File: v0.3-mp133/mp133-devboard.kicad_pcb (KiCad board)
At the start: 4 copper layers, 39.9 x 57.9 mm, 146 parts, among them CON1 microSDCon_SMT_104031-0811, J1 Pins_02x40_P0.4mm_W3.0mm_SMT, J2 Pins_02x40_P0.4mm_W3.0mm_SMT, J3 USB-C_Receptacle_Molex_217179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, J4 Pins_02x04_RightAngle_P2.54mm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, J5 Conn_01x02, J6 Pins_02x05_P1.27mm_SMT, U13 NCP51460SN33, U14 DDR3L-RAM-4Gb_MT41K256M16TW, U15 AP6230xZ6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

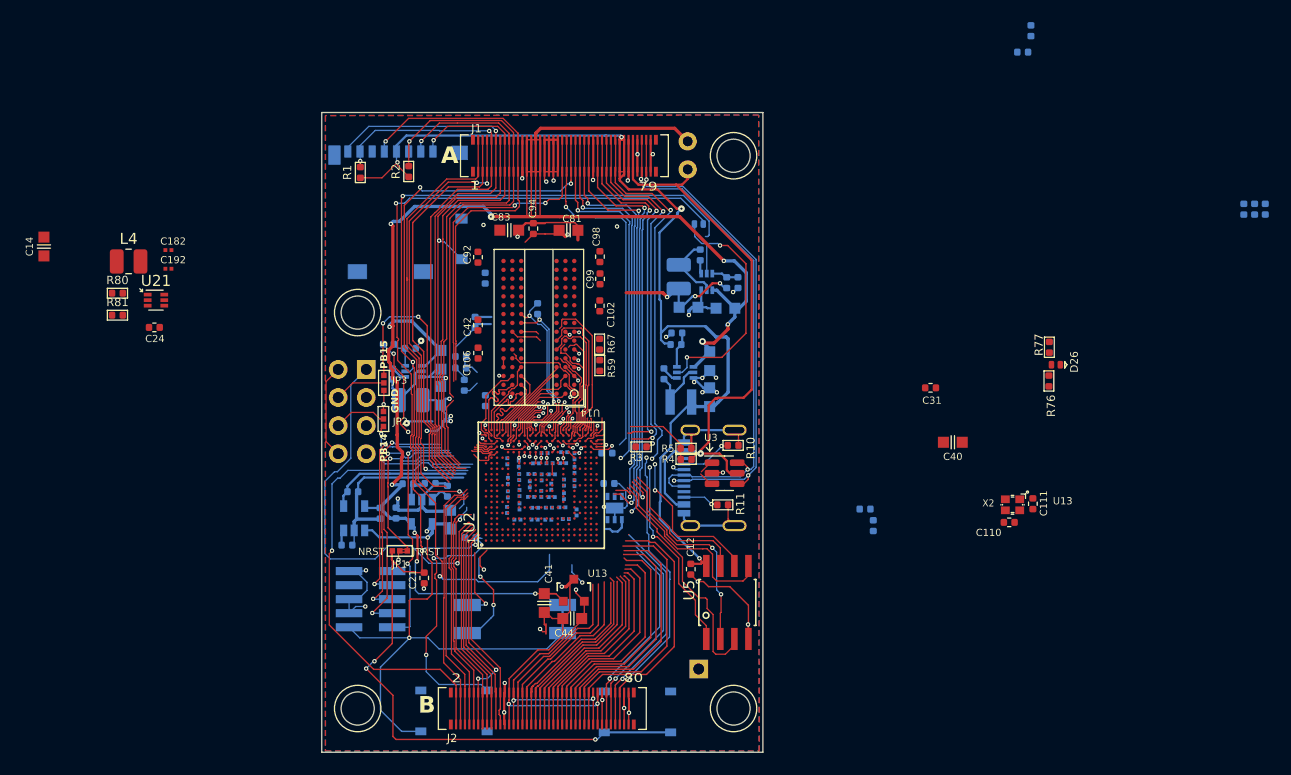
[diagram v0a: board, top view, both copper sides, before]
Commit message: mp13x: DDR3 RAM routed
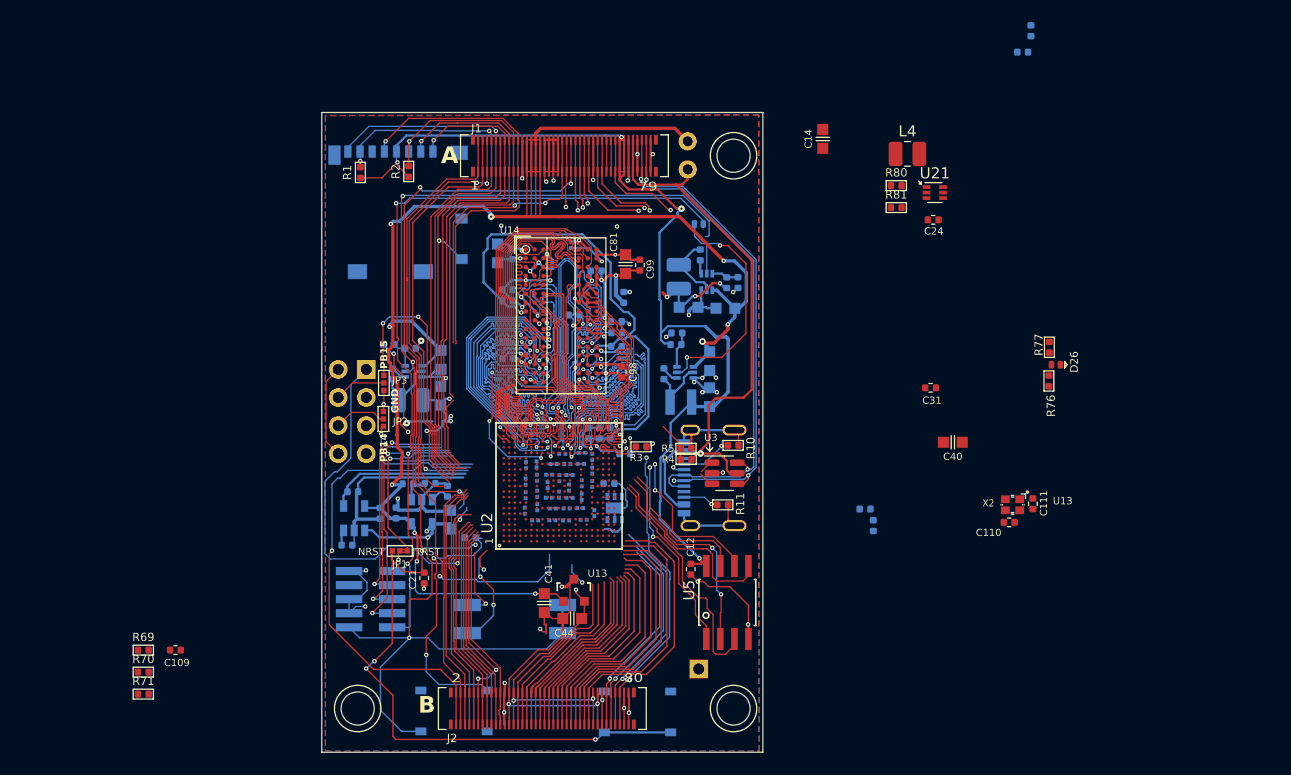
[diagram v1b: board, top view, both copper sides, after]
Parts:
- removed H2: Spacer Nylon, fits 3mm hole, 4ms_Hardware:MountingHole_Generic_3mm
- C102, C106, C182, C192, C42, C83, C92, C94, R59, R67: moved to B.Cu
- C109, R69, R70, R71: moved to F.Cu
- moved C14 71.1 mm to (234.5, 50.7)
- moved C24 71.1 mm to (244.5, 58.0)
- moved L4 71.1 mm to (242.1, 52.0)
- moved R80 71.1 mm to (241.1, 54.9)
- moved R81 71.1 mm to (241.1, 56.9)
- moved U21 71.1 mm to (244.6, 55.5)
- moved R78 62.6 mm to (215.2, 77.3)
- moved R79 62.6 mm to (214.2, 77.3)
- moved C13 62.6 mm to (213.3, 77.3)
- moved R71 41.9 mm to (173.0, 100.9)
- moved R70 38.9 mm to (173.0, 98.9), turned to 0 degrees
- moved R69 38.3 mm to (173.0, 96.9), turned to 0 degrees
- moved C182 36.4 mm to (211.7, 60.3), turned to -90 degrees
- moved C109 36.3 mm to (175.9, 96.9), turned to 0 degrees
- moved C192 34.7 mm to (210.0, 62.1), turned to 90 degrees
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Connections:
- C14 pad 2: +12V -> +5V
- U2 pad B21: /DDR_DQ2 -> /DDR_DQ0
- U2 pad D19: /DDR_DQ0 -> /DDR_DQ2
- U2 pad D20: /DDR_DQ7 -> /DDR_DQ5
- U2 pad F19: /DDR_DQ5 -> /DDR_DQ7
- U2 pad Y1: unconnected-(U2A-PA11-PadY1) -> /PA11
- U21 pad 1: +12V -> +5V
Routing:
- net VREF_DDR: track 8.46 -> 49.8 mm, vias 2 -> 3
- net /PD6: track 38.1 -> 5.88 mm, vias 2 -> 1
- net /PD12: track 33.0 -> 2.89 mm, vias 2 -> 0
- net /PE8: track 32.4 -> 2.89 mm, vias 2 -> 0
- net /PG10: track 38.5 -> 9.89 mm, vias 2 -> 1
- net GND: track 161.0 -> 189.3 mm, vias 49 -> 61
- net Net-(J1-Pin_57): track 37.7 -> 9.47 mm, vias 2 -> 1
- net Net-(J1-Pin_55): track 37.5 -> 9.50 mm, vias 2 -> 1
- net /PH12: track 33.3 -> 6.23 mm, vias 2 -> 1
- net /PE11: track 33.3 -> 6.47 mm, vias 2 -> 1
- net Net-(J1-Pin_41): track 32.2 -> 5.88 mm
- net /DDR_WEN: track 0.45 -> 25.2 mm, vias 1 -> 2
- net /DDR_A13: track 0.32 -> 25.0 mm, vias 1 -> 2
- net /DDR_A10: track 0.46 -> 24.9 mm, vias 1 -> 2
- net /DDR_CKE: track 0.95 -> 25.2 mm, vias 1 -> 2
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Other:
- board text added: "0"
- board text added: "0 mm"
- board text added: "0.01 mm"
- board text added: "0.02"
- board text added: "0.035 mm"
- board text added: "0.0900 mm / 0.0900 mm"
- board text added: "0.1 mm"
- board text added: "0.2000 mm"
- board text added: "1.24 mm"
- board text added: "1.6000 mm"
- board text added: "3.3"
- board text added: "39.9034 mm x 57.8692 mm"
- board text added: "4"
- board text added: "4.5"
- board text added: "B.Cu"
- board text added: "B.Mask"
- board text added: "B.Paste"
- board text added: "B.Silkscreen"
- board text added: "BOARD CHARACTERISTICS"
- board text added: "Board Thickness:"
- board text added: "Board overall dimensions:"
- board text added: "Bottom Silk Screen"
- board text added: "Bottom Solder Mask"
- board text added: "Bottom Solder Paste"
- board text added: "Castellated pads:"
- board text added: "Color"
- board text added: "Copper Finish:"
- board text added: "Copper Layer Count:"
- board text added: "Dielectric"
- board text added: "Edge card connectors:"
- board text added: "Epsilon R"
- board text added: "F.Cu"
- board text added: "F.Mask"
- board text added: "F.Paste"
- board text added: "F.Silkscreen"
- board text added: "FR4"
- board text added: "Impedance Control:"
- board text added: "In1.Cu"
- board text added: "In2.Cu"
- board text added: "Layer Name"
- board text added: "Loss Tangent"
- board text added: "Material"
- board text added: "Min hole diameter:"
- board text added: "Min track/spacing:"
- board text added: "No"
- board text added: "None"
- board text added: "Not specified"
- board text added: "Plated Board Edge:"
- board text added: "Thickness (mm)"
- board text added: "Top Silk Screen"
- board text added: "Top Solder Mask"
- board text added: "Top Solder Paste"
- board text added: "Type"
- board text added: "copper"
- board text added: "core"
- board text added: "prepreg"

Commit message: WIP Routing
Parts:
- added C1: 1uF_0201_4V, 4ms_Capacitor:C_0201, B.Cu at (213.7, 82.9)
- added H2: Spacer Nylon, fits 3mm hole, 4ms_Hardware:MountingHole_Generic_3mm, F.Cu at (192.4, 66.4)
- C109, C12, C14, C21, C24, C40, JP1, L4, R70, R71, R80, R81, U21, U5: moved to B.Cu
- moved R80 63.5 mm to (191.1, 93.9), turned to -90 degrees
- moved U21 63.4 mm to (192.4, 91.5), turned to -90 degrees
- moved C24 62.9 mm to (192.6, 93.5), turned to 180 degrees
- moved L4 61.8 mm to (195.0, 92.0), turned to 90 degrees
- moved R81 61.1 mm to (190.8, 91.5), turned to -90 degrees
- moved C14 57.6 mm to (191.5, 89.1), turned to 180 degrees
- moved C32 53.2 mm to (217.5, 80.3), turned to 180 degrees
- moved C40 52.6 mm to (194.8, 89.1), turned to 0 degrees
- moved C29 52.2 mm to (217.4, 81.4)
- moved R71 46.6 mm to (203.0, 65.2), turned to 180 degrees
- moved R70 46.4 mm to (204.5, 64.8), turned to 90 degrees
- moved C109 42.5 mm to (203.0, 64.2)
- moved R69 38.0 mm to (203.9, 74.8), turned to 90 degrees
- moved J6 31.0 mm to (224.5, 91.5)
- moved JP1 30.1 mm to (226.3, 87.1)
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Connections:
- J2 pad 35: Net-(J2-Pin_35) -> /PB1
- J2 pad 36: Net-(J2-Pin_35) -> /PB1
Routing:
- net /NRST: track 117.5 -> 12.0 mm, vias 6 -> 0
- net /UART_TX: track 35.9 -> 0.00 mm, vias 1 -> 0
- net GND: track 189.3 -> 222.7 mm, vias 61 -> 80
- net /PWR_ON: track 80.1 -> 50.3 mm
- net VDD_CPU: track 0.00 -> 26.2 mm, vias 0 -> 4
- net /DFU_BOOT: track 23.5 -> 0.01 mm, vias 2 -> 0
- net /JTCK_SWCLK: track 23.2 -> 0.00 mm, vias 2 -> 0
- net /JTDO_SWO: track 25.1 -> 3.38 mm, vias 3 -> 1
- net /PG1: track 18.8 -> 0.00 mm
- net /JTDI: track 21.0 -> 2.72 mm, vias 3 -> 1
- net VDD: track 60.6 -> 77.9 mm, vias 3 -> 16
- net /JTMS_SWDIO: track 21.5 -> 4.31 mm, vias 2 -> 0
- net /PH11: track 20.0 -> 2.89 mm, vias 2 -> 0
- net Net-(J2-Pin_35): track 16.9 -> 0.00 mm
- net /PB1: track 0.00 -> 16.9 mm
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- added copper zone on In1.Cu, net GND
- added copper zone on In2.Cu, net GND
- removed copper zone on In2.Cu, net VDD

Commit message: WIP routing
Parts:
- removed C30: 100nF_0402_16V, 4ms_Capacitor:C_0402
- C31, R76: moved to B.Cu
- C45, C72, C84, U18: moved to F.Cu
- moved R76 66.1 mm to (193.3, 96.6), turned to 180 degrees
- moved D26 65.1 mm to (191.9, 84.9)
- moved R77 64.5 mm to (192.0, 83.8), turned to 180 degrees
- moved TP1 42.1 mm to (227.0, 56.6)
- moved C110 41.3 mm to (210.3, 89.2), turned to -90 degrees
- moved C111 40.0 mm to (213.9, 89.0)
- moved X2 39.9 mm to (212.1, 89.1)
- moved R63 39.0 mm to (191.9, 95.0), turned to -90 degrees
- moved R64 38.9 mm to (191.3, 93.0), turned to -90 degrees
- moved C48 37.4 mm to (192.8, 91.1), turned to 180 degrees
- moved U16 35.5 mm to (193.9, 93.4), turned to -90 degrees
- moved C68 35.1 mm to (194.0, 95.3), turned to 180 degrees
- moved C72 35.0 mm to (225.8, 94.1), turned to 180 degrees
- moved C84 34.0 mm to (225.3, 89.3), turned to 0 degrees
- moved U18 33.7 mm to (225.2, 91.7)
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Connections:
- J2 pad 29: /PA0 -> /PA7
- J2 pad 30: /PA0 -> /PA7
- J2 pad 31: /PA1 -> /PA0
- J2 pad 32: /PA1 -> /PA0
- J2 pad 33: /PA2 -> /PA1
- J2 pad 34: /PA2 -> /PA1
- J2 pad 35: /PB1 -> /PA2
- J2 pad 36: /PB1 -> /PA2
- J2 pad 37: /PA4 -> /PA5
- J2 pad 38: /PA4 -> /PA5
- J2 pad 39: /PA5 -> /PF11
- J2 pad 40: /PA5 -> /PF11
- J2 pad 41: /PC0 -> /PA4
- J2 pad 42: /PC0 -> /PA4
- J2 pad 43: /PA7 -> /PC4
- J2 pad 44: /PA7 -> /PC4
- J2 pad 45: /PC1 -> /PC5
- J2 pad 46: /PC1 -> /PC5
- J2 pad 47: /PC2 -> /PB1
- J2 pad 48: /PC2 -> /PB1
- J2 pad 49: /PC4 -> /PC1
- J2 pad 50: /PC4 -> /PC1
- J2 pad 51: /PC5 -> /PG13
- J2 pad 52: /PC5 -> /PG13
- J2 pad 61: /PB0 -> /PC2
- J2 pad 62: /PB0 -> /PC2
- U2 pad U3: GNDADC -> GND
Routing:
- net /NRST: track 12.0 -> 99.2 mm, vias 0 -> 2
- net /PWR_ON: track 50.3 -> 81.0 mm, vias 3 -> 4
- net Net-(U2D-PWR_CPU_ON): track 0.00 -> 29.5 mm, vias 0 -> 2
- net GNDADC: track 42.1 -> 70.5 mm, vias 2 -> 6
- net /PG13: track 0.00 -> 28.2 mm
- net +3V3: track 81.8 -> 108.1 mm, vias 3 -> 6
- net /PB0: track 25.5 -> 0.00 mm
- net /PF11: track 0.00 -> 25.5 mm
- net /DEBUG2: track 24.2 -> 0.00 mm, vias 2 -> 0
- net /JTRST: track 4.46 -> 26.5 mm, vias 0 -> 1
- net GND: track 222.7 -> 243.8 mm, vias 80 -> 87
- net Net-(J1-Pin_39): track 26.9 -> 6.89 mm, vias 2 -> 1
- net Net-(J2-Pin_1): track 43.7 -> 23.8 mm, vias 1 -> 0
- net /JTCK_SWCLK: track 0.00 -> 19.3 mm, vias 0 -> 1
- net /PC0: track 17.4 -> 0.00 mm
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- removed copper zone on In2.Cu, net VDD_CORE
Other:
- board text added: "0 2"
- board text removed: "2 0"
- board text removed: "Debug"
- board text removed: "U13"
- board text removed: "U20"

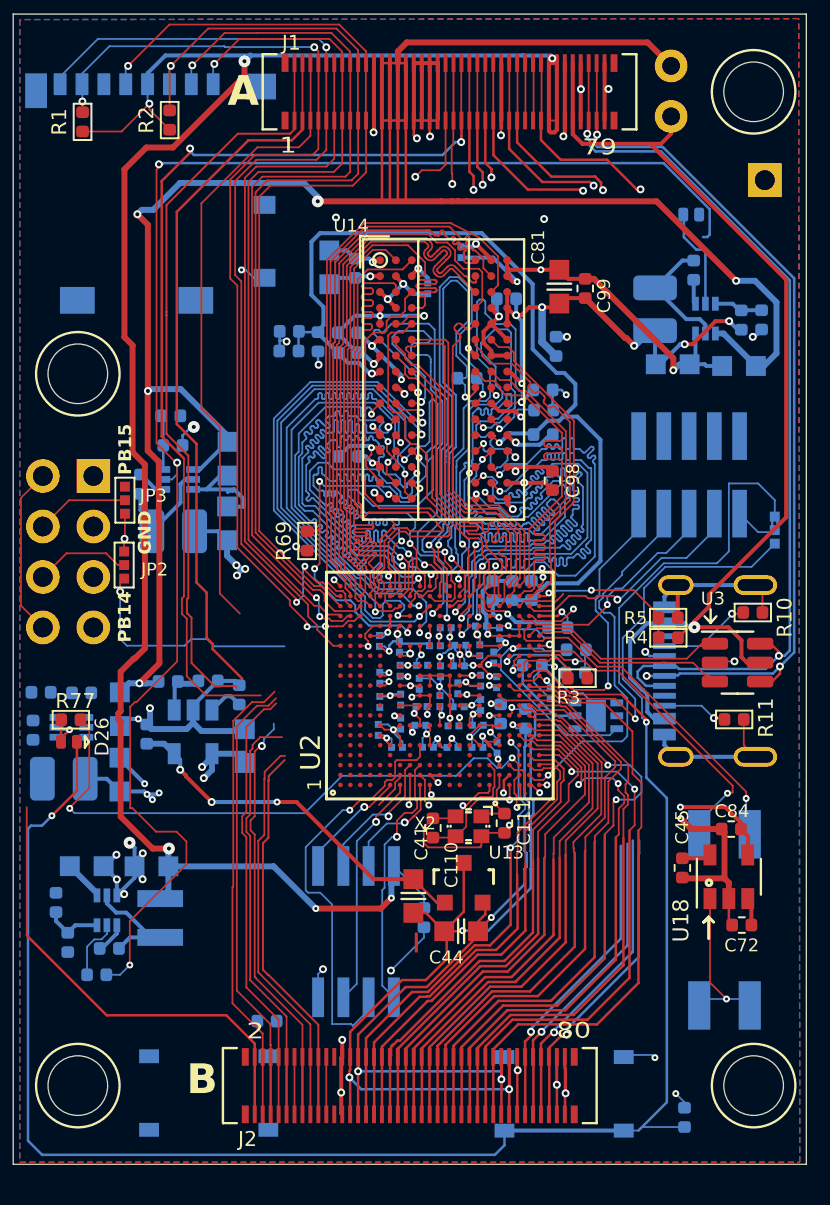
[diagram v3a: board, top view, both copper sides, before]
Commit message: mp133: WIP routing and pin assignment
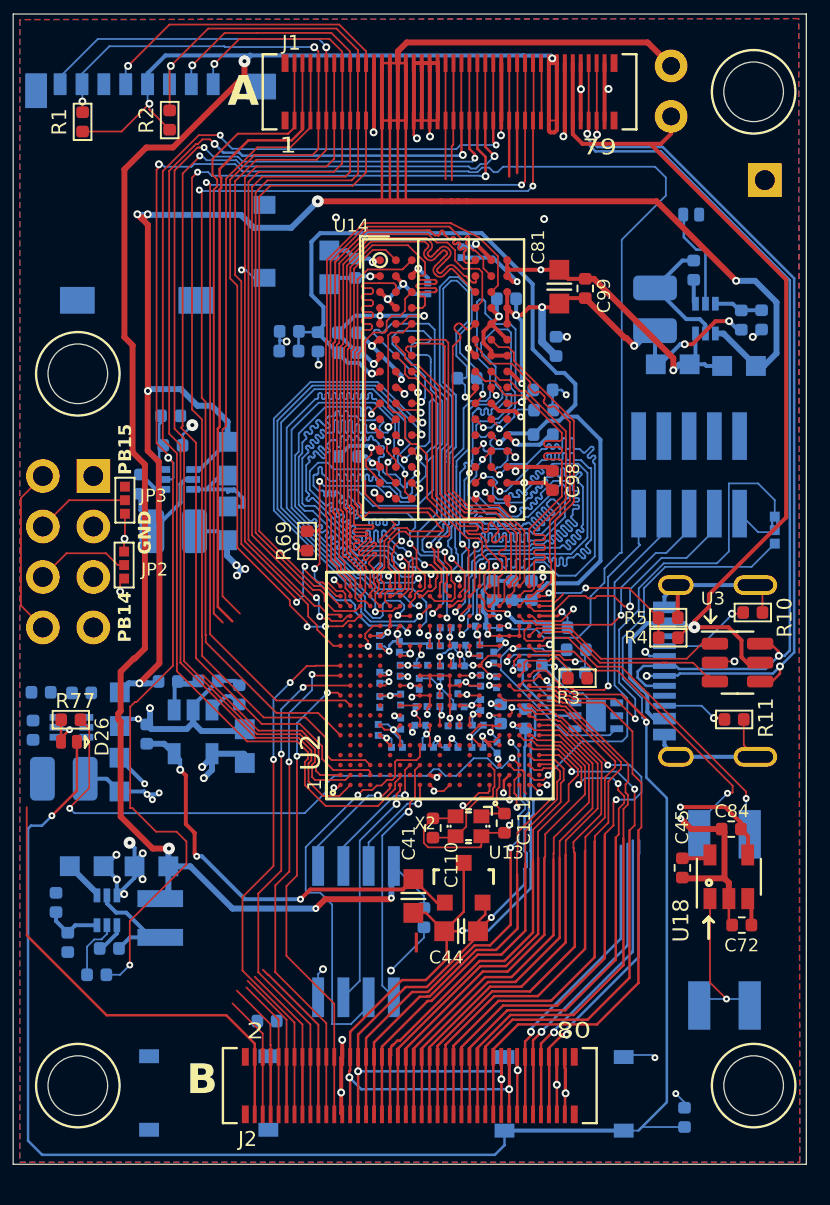
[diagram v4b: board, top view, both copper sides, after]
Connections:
- J2 pad 11: /PH11 -> /PF3
- J2 pad 12: /PH11 -> /PF3
- J2 pad 15: /PA8 -> /PF1
- J2 pad 16: /PA8 -> /PF1
- J2 pad 19: /PH6 -> /PH13
- J2 pad 20: /PH6 -> /PH13
- J2 pad 21: /PG1 -> /PG7
- J2 pad 22: /PG1 -> /PG7
- U2 pad A10: unconnected-(U2B-PG7-PadA10) -> /PG7
- U2 pad A12: unconnected-(U2B-PH13-PadA12) -> /PH13
- U2 pad A13: unconnected-(U2B-PF3-PadA13) -> /PF3
- U2 pad B11: unconnected-(U2B-PF1-PadB11) -> /PF1
- U2 pad N3: unconnected-(U2B-PH6-PadN3) -> /PH6
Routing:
- net /PD6: track 5.88 -> 57.9 mm, vias 1 -> 2
- net /PG10: track 11.8 -> 63.7 mm, vias 1 -> 2
- net /PD12: track 2.89 -> 54.7 mm, vias 0 -> 2
- net /PE11: track 6.47 -> 57.7 mm, vias 1 -> 2
- net /PE8: track 2.89 -> 53.5 mm, vias 0 -> 2
- net /PH12: track 6.23 -> 56.3 mm, vias 1 -> 2
- net /PF3: track 0.00 -> 26.7 mm, vias 0 -> 2
- net /PF1: track 0.00 -> 25.9 mm, vias 0 -> 2
- net /PH13: track 0.00 -> 25.5 mm, vias 0 -> 2
- net /PG7: track 0.00 -> 23.8 mm, vias 0 -> 2
- net /PWR_ON: track 81.0 -> 103.3 mm
- net /PA8: track 19.8 -> 0.00 mm
- net Net-(J2-Pin_3): track 23.2 -> 6.31 mm
- net Net-(J2-Pin_5): track 22.9 -> 7.03 mm
- net Net-(J2-Pin_7): track 22.4 -> 7.15 mm
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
